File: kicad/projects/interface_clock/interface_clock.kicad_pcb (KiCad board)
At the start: 2 copper layers, 203.2 x 97.8 mm, 77 parts, among them J1 Control_signal_backplane, J10 Conn_01x02_Female, J2 Aux_connection, J3 Bus_connection, J4 MAR_content_in, J5 EXT_BUS, J6 CONTROL_INPUTS, J7 CLOCK_RWMEM_OUT, J8 EXT_ADDR, J9 Conn_01x03_Male, U1 74HC02, U10 74HC157, U11 74HC14, U12 74HC245, U13 74HC126, U14 74HC109, U2 74HC04, U3 74HC08, U4 74HC08, U5 74HC02, U6 74HC245, U7 74HC245, U8 74HC245, U9 74HC245, X1 CXO_DIP8

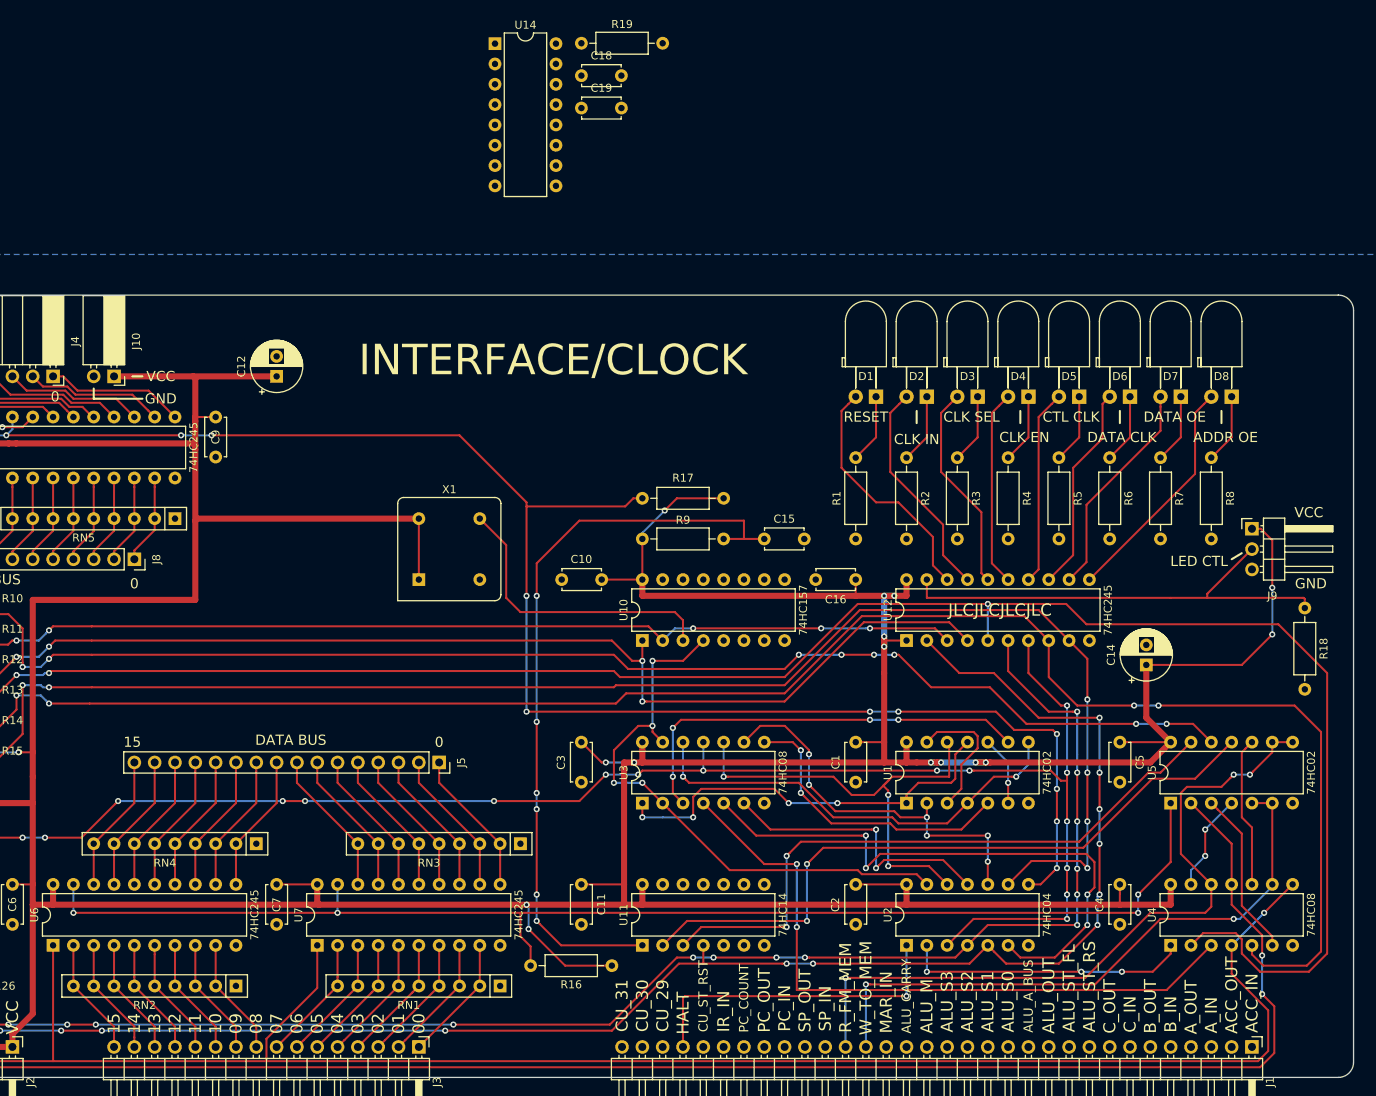
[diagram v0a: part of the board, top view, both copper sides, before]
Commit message: Finish wiring on interface.
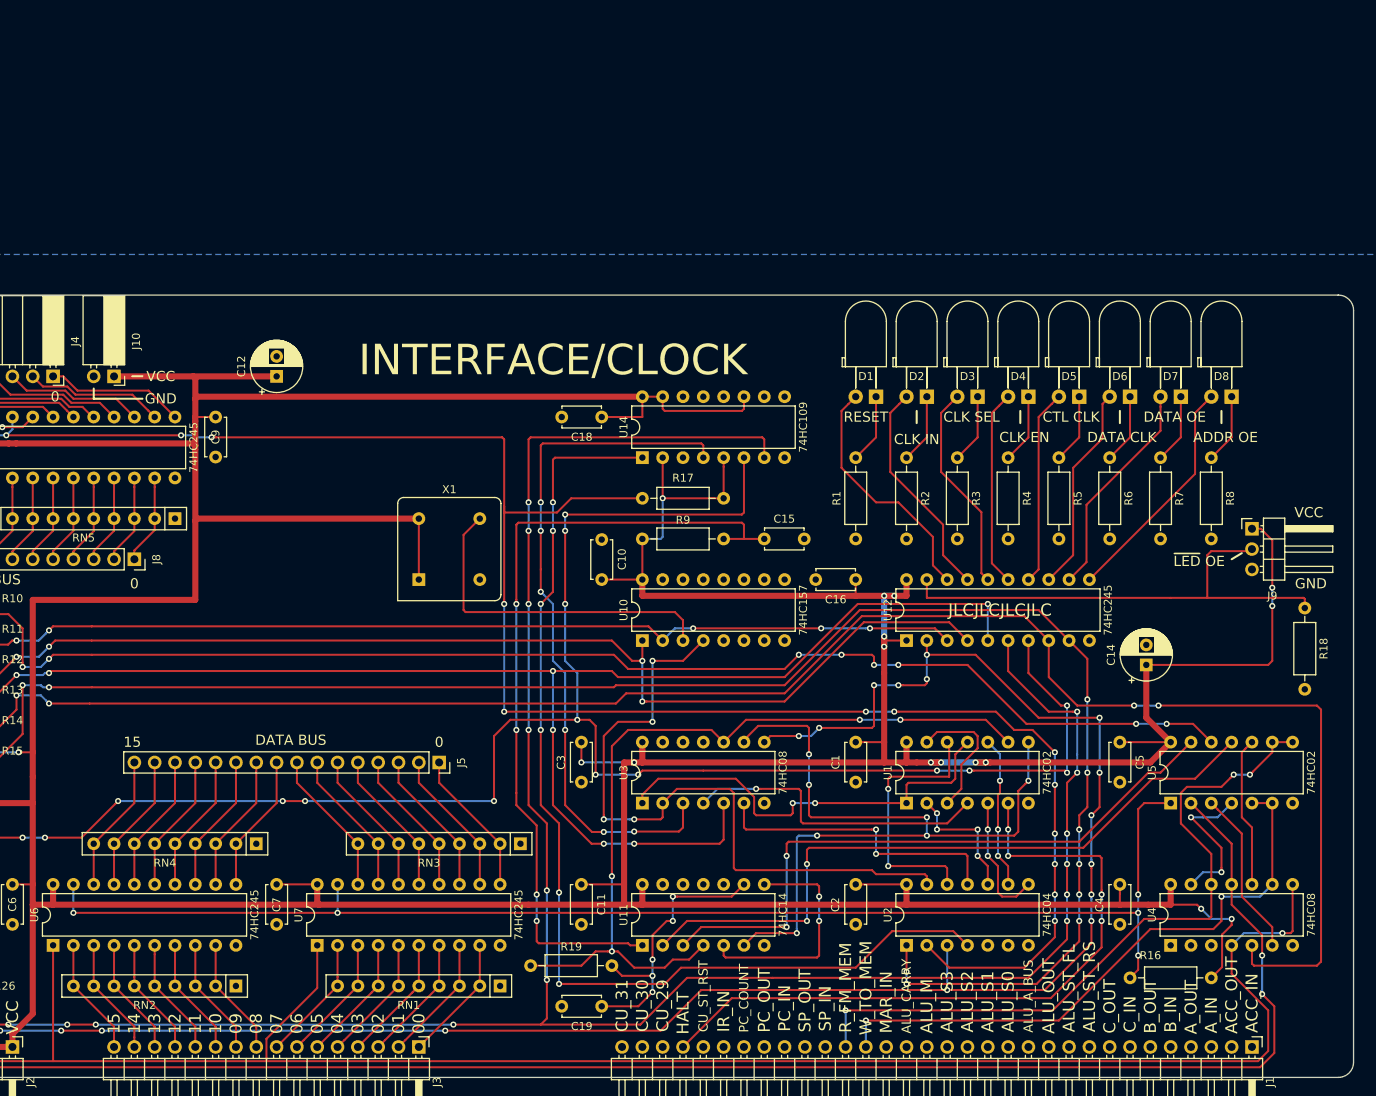
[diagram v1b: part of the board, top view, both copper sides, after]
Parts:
- moved R19 115.5 mm to (151.1, 134.6)
- moved C19 112.3 mm to (160.0, 139.7), turned to 180 degrees
- moved R16 74.9 mm to (236.2, 136.1)
- moved U14 54.9 mm to (165.1, 71.1), turned to 90 degrees
- moved C18 42.7 mm to (160.0, 66.0), turned to 180 degrees
- turned C10 to 90 degrees
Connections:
- U2 pad 1: Net-(U1-Pad10) -> /ADDRESS_BUS_OUTPUT_ENABLE
- U2 pad 2: /CLK_EN_FROM_RESET -> /~ADDRESS_BUS_OUTPUT_ENABLE
- U2 pad 8: /~ADDRESS_BUS_OUTPUT_ENABLE -> /CLK_EN_FROM_RESET
- U2 pad 9: /ADDRESS_BUS_OUTPUT_ENABLE -> Net-(U1-Pad10)
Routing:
- net Net-(U14-Pad1): track 0.00 -> 132.9 mm, vias 0 -> 6
- net /UNBUF_CTL_CLK: track 199.3 -> 306.0 mm, vias 14 -> 16
- net /RESET_PWRUP: track 0.00 -> 103.3 mm, vias 0 -> 4
- net VCC: track 755.7 -> 852.6 mm
- net Net-(U1-Pad8): track 0.00 -> 96.1 mm, vias 0 -> 7
- net Net-(U3-Pad4): track 84.7 -> 0.00 mm, vias 2 -> 0
- net Net-(U2-Pad6): track 73.7 -> 0.00 mm, vias 4 -> 0
- net /CLK_ENABLE: track 263.0 -> 205.2 mm, vias 3 -> 7
- net /HALT: track 40.5 -> 87.0 mm, vias 1 -> 4
- net Net-(U1-Pad5): track 37.0 -> 0.00 mm, vias 2 -> 0
- net Net-(U2-Pad2): track 35.8 -> 0.00 mm, vias 3 -> 0
- net Net-(C19-Pad1): track 0.00 -> 35.7 mm, vias 0 -> 5
- net /SCE_OUT: track 53.4 -> 87.7 mm, vias 4 -> 6
- net /RESET: track 220.6 -> 253.7 mm, vias 12 -> 17
- net Net-(U1-Pad2): track 48.8 -> 16.3 mm, vias 6 -> 4
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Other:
- board text added: "~LED OE"
- board text removed: "LED CTL"

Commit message: Last bits of labelling and re-routing on interface-clock
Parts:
- moved R10 5.59 mm to (88.1, 88.9)
- moved R11 5.59 mm to (88.1, 92.7)
- moved R12 5.59 mm to (88.1, 96.5)
- moved R13 5.59 mm to (88.1, 100.3)
- moved R14 5.59 mm to (88.1, 104.1)
- moved R15 5.59 mm to (88.1, 108.0)
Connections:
- U14 pad 12: GND -> VCC
- U14 pad 14: GND -> VCC
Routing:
- net (no net): track 390.1 -> 0.00 mm
- net VCC: track 852.6 -> 862.2 mm
- net /CTL_CLK: track 26.9 -> 34.0 mm
- net /UNBUF_CTL_CLK: track 306.0 -> 309.3 mm
- net /DATA_CLK: track 32.4 -> 35.0 mm
- net /UNBUF_DATA_CLK: track 241.1 -> 243.5 mm
- net /EXT_RESET: track 191.3 -> 190.7 mm

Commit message: Tech checks on interface, some of program counter.
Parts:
- moved J9 1.27 mm to (241.3, 78.7)
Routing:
- net VCC: track 862.2 -> 864.1 mm
- net /EXT_RESET: track 190.7 -> 189.1 mm
- net /CLOCK_SEL: track 162.3 -> 163.5 mm
- net /CLK_ENABLE: track 205.2 -> 206.2 mm
- net /DATA_BUS_OUTPUT_ENABLE: track 250.7 -> 249.7 mm
- net /EXT_CLK_IN: track 147.3 -> 147.9 mm
- net /LED_CONTROL: track 62.0 -> 61.4 mm
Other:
- board text added: "LED ~OE"
- board text removed: "~LED OE"

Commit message: Program counter tech checks complete, starting IDC addition to interface.
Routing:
- net VCC: track 864.1 -> 856.8 mm
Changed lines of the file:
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@@
     (thickness 1.6)
     (drawings 126)
-    (tracks 1365)
+    (tracks 1359)
     (zones 0)
     (modules 77)
@@
   )
   (setup
-    (last_trace_width 0.254)
+    (last_trace_width 0.762)
     (user_trace_width 0.762)
     (trace_clearance 0.2)
@@
   (segment (start 198.12 106.68) (end 198.12 109.22) (width 0.762) (layer F.Cu) (net 2))
   (segment (start 198.12 109.22) (end 199.39 109.22) (width 0.762) (layer F.Cu) (net 2))
-  (segment (start 85.898239 69.342009) (end 85.89823 69.342) (width 0.762) (layer F.Cu) (net 2))
-  (segment (start 109.22 69.596) (end 108.966 69.342) (width 0.762) (layer F.Cu) (net 2))
-  (segment (start 53.34 69.195998) (end 53.34 66.04) (width 0.762) (layer F.Cu) (net 2))
-  (segment (start 108.966 69.342) (end 86.82177 69.342) (width 0.762) (layer F.Cu) (net 2))
-  (segment (start 53.486002 69.342) (end 53.34 69.195998) (width 0.762) (layer F.Cu) (net 2))
-  (segment (start 86.82177 69.342) (end 86.821761 69.342009) (width 0.762) (layer F.Cu) (net 2))
-  (segment (start 86.821761 69.342009) (end 85.898239 69.342009) (width 0.762) (layer F.Cu) (net 2))
   (segment (start 198.12 86.36) (end 198.12 88.392) (width 0.762) (layer F.Cu) (net 2))
   (segment (start 165.1 88.392) (end 165.1 86.36) (width 0.762) (layer F.Cu) (net 2))
@@
   (segment (start 108.966 60.96) (end 109.22 61.214) (width 0.762) (layer F.Cu) (net 2))
   (segment (start 109.22 70.104) (end 109.22 69.596) (width 0.762) (layer F.Cu) (net 2))
-  (segment (start 119.38 60.96) (end 108.966 60.96) (width 0.762) (layer F.Cu) (net 2))
   (segment (start 88.9 127) (end 88.9 124.46) (width 0.762) (layer F.Cu) (net 2))
   (segment (start 86.36 124.46) (end 88.9 124.46) (width 0.254) (layer F.Cu) (net 2))
@@
   (segment (start 160.02 86.36) (end 165.1 86.36) (width 0.254) (layer F.Cu) (net 2))
   (segment (start 165.1 81.28) (end 165.1 86.36) (width 0.254) (layer F.Cu) (net 2))
-  (segment (start 53.34 83.82) (end 53.34 76.962) (width 0.254) (layer F.Cu) (net 2))
-  (segment (start 53.34 76.962) (end 54.61 75.692) (width 0.254) (layer F.Cu) (net 2))
-  (segment (start 54.61 75.692) (end 54.61 69.342) (width 0.254) (layer F.Cu) (net 2))
-  (segment (start 54.61 69.342) (end 53.486002 69.342) (width 0.762) (layer F.Cu) (net 2))
   (segment (start 111.76 66.04) (end 109.22 66.04) (width 0.254) (layer F.Cu) (net 2))
   (segment (start 109.22 66.04) (end 109.22 66.548) (width 0.762) (layer F.Cu) (net 2))
@@
   (segment (start 88.138 107.95) (end 92.71 107.95) (width 0.254) (layer B.Cu) (net 2))
   (segment (start 109.22 66.548) (end 109.22 69.596) (width 0.762) (layer F.Cu) (net 2))
-  (segment (start 83.82 66.04) (end 83.82 69.342) (width 0.762) (layer F.Cu) (net 2))
-  (segment (start 85.89823 69.342) (end 83.82 69.342) (width 0.762) (layer F.Cu) (net 2))
-  (segment (start 83.82 69.342) (end 54.61 69.342) (width 0.762) (layer F.Cu) (net 2))
   (segment (start 124.714 127) (end 150.876 127) (width 0.762) (layer F.Cu) (net 2))
   (segment (start 162.814 127) (end 150.876 127) (width 0.762) (layer F.Cu) (net 2))
@@
   (segment (start 109.22 63.754) (end 109.22 66.04) (width 0.762) (layer F.Cu) (net 2))
   (segment (start 109.22 61.214) (end 109.22 63.754) (width 0.762) (layer F.Cu) (net 2))
-  (segment (start 109.474 63.5) (end 165.1 63.5) (width 0.762) (layer F.Cu) (net 2))
   (segment (start 175.26 71.12) (end 175.26 72.25137) (width 0.254) (layer F.Cu) (net 2))
   (segment (start 175.26 72.25137) (end 175.26 76.2) (width 0.254) (layer F.Cu) (net 2))
@@
   (segment (start 243.586 78.74) (end 241.3 78.74) (width 0.254) (layer F.Cu) (net 2))
   (segment (start 243.84 78.994) (end 243.586 78.74) (width 0.254) (layer F.Cu) (net 2))
+  (segment (start 83.82 69.85) (end 83.82 66.04) (width 0.762) (layer F.Cu) (net 2))
+  (segment (start 53.34 69.85) (end 53.34 66.04) (width 0.762) (layer F.Cu) (net 2))
+  (segment (start 108.966 69.85) (end 53.34 69.85) (width 0.762) (layer F.Cu) (net 2))
+  (segment (start 109.22 69.596) (end 108.966 69.85) (width 0.762) (layer F.Cu) (net 2))
+  (segment (start 54.61 75.692) (end 54.61 69.85) (width 0.254) (layer F.Cu) (net 2))
+  (segment (start 53.34 83.82) (end 53.34 76.962) (width 0.254) (layer F.Cu) (net 2))
+  (segment (start 53.34 76.962) (end 54.61 75.692) (width 0.254) (layer F.Cu) (net 2))
+  (segment (start 119.38 63.5) (end 119.38 60.96) (width 0.762) (layer F.Cu) (net 2))
+  (segment (start 119.38 63.5) (end 165.1 63.5) (width 0.762) (layer F.Cu) (net 2))
+  (segment (start 109.474 63.5) (end 119.38 63.5) (width 0.762) (layer F.Cu) (net 2))
   (via (at 210.82 120.903994) (size 0.762) (drill 0.4) (layers F.Cu B.Cu) (net 6))
   (segment (start 210.82 114.3) (end 210.82 117.602) (width 0.254) (layer F.Cu) (net 6))
@@
   (segment (start 71.12 60.96) (end 71.969999 61.809999) (width 0.254) (layer F.Cu) (net 64))
   (segment (start 71.969999 61.809999) (end 76.2 66.04) (width 0.254) (layer F.Cu) (net 64))
-  (segment (start 87.63 67.31) (end 88.9 66.04) (width 0.254) (layer F.Cu) (net 65))
-  (via (at 85.09 67.31) (size 0.762) (drill 0.4) (layers F.Cu B.Cu) (net 65))
-  (segment (start 85.09 67.31) (end 87.63 67.31) (width 0.254) (layer F.Cu) (net 65))
-  (via (at 82.550016 67.31) (size 0.762) (drill 0.4) (layers F.Cu B.Cu) (net 65))
-  (segment (start 85.09 67.31) (end 82.550016 67.31) (width 0.254) (layer B.Cu) (net 65))
-  (segment (start 80.01 67.31) (end 82.550016 67.31) (width 0.254) (layer F.Cu) (net 65))
-  (segment (start 73.66 60.96) (end 80.01 67.31) (width 0.254) (layer F.Cu) (net 65))
+  (segment (start 80.264 67.564) (end 82.550016 67.564) (width 0.254) (layer F.Cu) (net 65))
+  (segment (start 73.66 60.96) (end 80.264 67.564) (width 0.254) (layer F.Cu) (net 65))
+  (via (at 82.550016 67.564) (size 0.762) (drill 0.4) (layers F.Cu B.Cu) (net 65))
+  (via (at 85.09 67.564) (size 0.762) (drill 0.4) (layers F.Cu B.Cu) (net 65))
+  (segment (start 82.550016 67.564) (end 85.09 67.564) (width 0.254) (layer B.Cu) (net 65))
+  (segment (start 87.376 67.564) (end 85.09 67.564) (width 0.254) (layer F.Cu) (net 65))
+  (segment (start 88.9 66.04) (end 87.376 67.564) (width 0.254) (layer F.Cu) (net 65))
   (segment (start 90.640001 65.240001) (end 91.44 66.04) (width 0.254) (layer F.Cu) (net 66))
   (segment (start 90.17 64.77) (end 90.640001 65.240001) (width 0.254) (layer F.Cu) (net 66))
@@
   (segment (start 77.978 106.172) (end 89.154 106.172) (width 0.254) (layer F.Cu) (net 155))
   (segment (start 89.154 106.172) (end 91.948 103.378) (width 0.254) (layer F.Cu) (net 155))
-  (segment (start 86.36 67.563998) (end 85.59799 68.326008) (width 0.254) (layer B.Cu) (net 156))
-  (via (at 85.59799 68.326008) (size 0.762) (drill 0.4) (layers F.Cu B.Cu) (net 156))
-  (segment (start 86.36 66.04) (end 86.36 67.563998) (width 0.254) (layer B.Cu) (net 156))
-  (via (at 81.787978 68.326) (size 0.762) (drill 0.4) (layers F.Cu B.Cu) (net 156))
-  (segment (start 81.28 68.326) (end 81.787978 68.326) (width 0.254) (layer F.Cu) (net 156))
-  (segment (start 58.166 68.326) (end 81.787978 68.326) (width 0.254) (layer F.Cu) (net 156))
-  (segment (start 55.88 66.04) (end 58.166 68.326) (width 0.254) (layer F.Cu) (net 156))
-  (segment (start 85.597982 68.326) (end 85.59799 68.326008) (width 0.254) (layer B.Cu) (net 156))
-  (segment (start 81.787978 68.326) (end 85.597982 68.326) (width 0.254) (layer B.Cu) (net 156))
   (via (at 216.662 112.014) (size 0.762) (drill 0.4) (layers F.Cu B.Cu) (net 156))
   (via (at 216.662 118.11) (size 0.762) (drill 0.4) (layers F.Cu B.Cu) (net 156))
@@
   (segment (start 165.1 76.2) (end 156.21 76.2) (width 0.254) (layer F.Cu) (net 156))
   (segment (start 156.21 76.2) (end 154.432 77.978) (width 0.254) (layer F.Cu) (net 156))
-  (segment (start 107.695992 68.326008) (end 107.696 68.326) (width 0.254) (layer F.Cu) (net 156))
   (via (at 107.696 68.326) (size 0.762) (drill 0.4) (layers F.Cu B.Cu) (net 156))
-  (segment (start 85.59799 68.326008) (end 107.695992 68.326008) (width 0.254) (layer F.Cu) (net 156))
   (via (at 111.252 68.326) (size 0.762) (drill 0.4) (layers F.Cu B.Cu) (net 156))
   (segment (start 107.696 68.326) (end 111.252 68.326) (width 0.254) (layer B.Cu) (net 156))
@@
   (segment (start 147.828 77.216) (end 147.828 68.834) (width 0.254) (layer F.Cu) (net 156))
   (segment (start 147.828 68.834) (end 147.32 68.326) (width 0.254) (layer F.Cu) (net 156))
+  (segment (start 81.249185 68.58) (end 81.788 68.58) (width 0.254) (layer F.Cu) (net 156))
+  (segment (start 58.42 68.58) (end 81.249185 68.58) (width 0.254) (layer F.Cu) (net 156))
+  (segment (start 55.88 66.04) (end 58.42 68.58) (width 0.254) (layer F.Cu) (net 156))
+  (via (at 81.788 68.58) (size 0.762) (drill 0.4) (layers F.Cu B.Cu) (net 156))
+  (segment (start 81.788 68.58) (end 82.326815 68.58) (width 0.254) (layer B.Cu) (net 156))
+  (segment (start 82.326815 68.58) (end 85.598 68.58) (width 0.254) (layer B.Cu) (net 156))
+  (segment (start 85.852 68.326) (end 85.598 68.58) (width 0.254) (layer F.Cu) (net 156))
+  (segment (start 107.696 68.326) (end 85.852 68.326) (width 0.254) (layer F.Cu) (net 156))
+  (segment (start 86.36 66.04) (end 86.36 67.818) (width 0.254) (layer B.Cu) (net 156))
+  (segment (start 86.36 67.818) (end 85.598 68.58) (width 0.254) (layer B.Cu) (net 156))
+  (via (at 85.598 68.58) (size 0.762) (drill 0.4) (layers F.Cu B.Cu) (net 156))
   (via (at 227.076 125.73) (size 0.762) (drill 0.4) (layers F.Cu B.Cu) (net 157))
   (via (at 127 128.016) (size 0.762) (drill 0.4) (layers F.Cu B.Cu) (net 157))

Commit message: Tech check on interface done.
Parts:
- C15: value 0.1uF -> 4.7uF
- C19: value C -> 4.7uF
- J5: value EXT_BUS -> EXT BUS; footprint Connector_PinSocket_2.54mm:PinSocket_1x16_P2.54mm_Vertical -> Connector_PinHeader_2.54mm:PinHeader_2x17_P2.54mm_Vertical
- J8: value EXT_ADDR -> EXT ADDR; footprint Connector_PinSocket_2.54mm:PinSocket_1x16_P2.54mm_Vertical -> Connector_PinHeader_2.54mm:PinHeader_2x17_P2.54mm_Vertical
- R1, R3, R4, R7, R8: value R_US -> 1K
- R10, R11, R12, R13, R14, R15, R19, R9: value R_US -> 10K
- R2, R5, R6: value R_US -> 2K
- moved J5 5.08 mm to (144.8, 109.2)
- moved C6 5.08 mm to (86.4, 129.5)
- moved C17 4.02 mm to (82.5, 120.7), turned to 270 degrees
- moved R11 3.81 mm to (88.1, 96.5)
- moved R12 3.81 mm to (88.1, 100.3)
- moved R13 3.81 mm to (88.1, 104.1)
- moved R14 3.81 mm to (88.1, 108.0)
- moved R15 3.81 mm to (88.1, 111.8)
- moved R10 3.81 mm to (88.1, 92.7)
- moved C19 2.54 mm to (157.5, 139.7), turned to 270 degrees
- moved C8 1.80 mm to (54.6, 82.5), turned to 270 degrees
- moved J6 1.27 mm to (61.0, 94.0)
- moved J8 1.27 mm to (101.6, 85.1)
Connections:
- net /ADDR_BUS_OE renamed /ADDR_BUS_OE_LED
- net /CLK_EN_FROM_RESET renamed /~CLK_EN_FROM_RESET
- J5 pad 10: /EXT_BUS_09 -> GND
- J5 pad 11: /EXT_BUS_10 -> /EXT_BUS_05
- J5 pad 12: /EXT_BUS_11 -> GND
- J5 pad 13: /EXT_BUS_12 -> /EXT_BUS_06
- J5 pad 14: /EXT_BUS_13 -> GND
- J5 pad 15: /EXT_BUS_14 -> /EXT_BUS_07
- J5 pad 16: /EXT_BUS_15 -> GND
- J5 pad 2: /EXT_BUS_01 -> GND
- J5 pad 3: /EXT_BUS_02 -> /EXT_BUS_01
- J5 pad 4: /EXT_BUS_03 -> GND
- J5 pad 5: /EXT_BUS_04 -> /EXT_BUS_02
- J5 pad 6: /EXT_BUS_05 -> GND
- J5 pad 7: /EXT_BUS_06 -> /EXT_BUS_03
- J5 pad 8: /EXT_BUS_07 -> GND
- J5 pad 9: /EXT_BUS_08 -> /EXT_BUS_04
- J8 pad 10: /EXT_ADDR_09 -> GND
- J8 pad 11: /EXT_ADDR_10 -> /EXT_ADDR_05
- J8 pad 12: /EXT_ADDR_11 -> GND
- J8 pad 13: /EXT_ADDR_12 -> /EXT_ADDR_06
- J8 pad 14: /EXT_ADDR_13 -> GND
- J8 pad 15: /EXT_ADDR_14 -> /EXT_ADDR_07
- J8 pad 16: /EXT_ADDR_15 -> GND
- J8 pad 2: /EXT_ADDR_01 -> GND
- J8 pad 3: /EXT_ADDR_02 -> /EXT_ADDR_01
- J8 pad 4: /EXT_ADDR_03 -> GND
- J8 pad 5: /EXT_ADDR_04 -> /EXT_ADDR_02
- J8 pad 6: /EXT_ADDR_05 -> GND
- J8 pad 7: /EXT_ADDR_06 -> /EXT_ADDR_03
- J8 pad 8: /EXT_ADDR_07 -> GND
- J8 pad 9: /EXT_ADDR_08 -> /EXT_ADDR_04
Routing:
- net /EXT_BUS_08: track 17.3 -> 23.3 mm
- net /~ADDRESS_BUS_OUTPUT_ENABLE: track 261.8 -> 256.6 mm
- net VCC: track 856.8 -> 852.1 mm
- net /ADDRESS_BUS_OUTPUT_ENABLE: track 242.5 -> 246.9 mm, vias 10 -> 11
- net /EXT_BUS_15: track 17.3 -> 21.2 mm
- net /CLK_ENABLE: track 206.2 -> 210.1 mm, vias 7 -> 8
- net /CLOCK_SEL: track 163.5 -> 167.2 mm, vias 4 -> 5
- net /EXT_BUS_12: track 17.3 -> 20.9 mm
- net /DATA_BUS_OUTPUT_ENABLE: track 249.7 -> 253.2 mm, vias 4 -> 5
- net /EXT_BUS_14: track 17.3 -> 20.8 mm
- net /EXT_BUS_11: track 17.3 -> 20.8 mm
- net /EXT_BUS_10: track 17.3 -> 20.8 mm
- net /EXT_BUS_13: track 17.3 -> 20.8 mm
- net /EXT_CLK_IN: track 147.9 -> 151.3 mm, vias 5 -> 6
- net /EXT_BUS_09: track 17.3 -> 20.6 mm
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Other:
- board text added: "SIGNAL"
- board text added: "V.2"
- board text added: "x"
